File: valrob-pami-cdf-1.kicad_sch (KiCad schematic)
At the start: 111 parts, among them J1 Conn_01x04, J10 Conn_01x04_Pin, J3 USB_C_Receptacle_USB2.0_14P, J4 Conn_01x02, M1 Motor_Servo, Q1 Q_NMOS, Q2 Q_NMOS, Q3 Q_NMOS, SW1 SW_SPST, SW3 SW_Push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

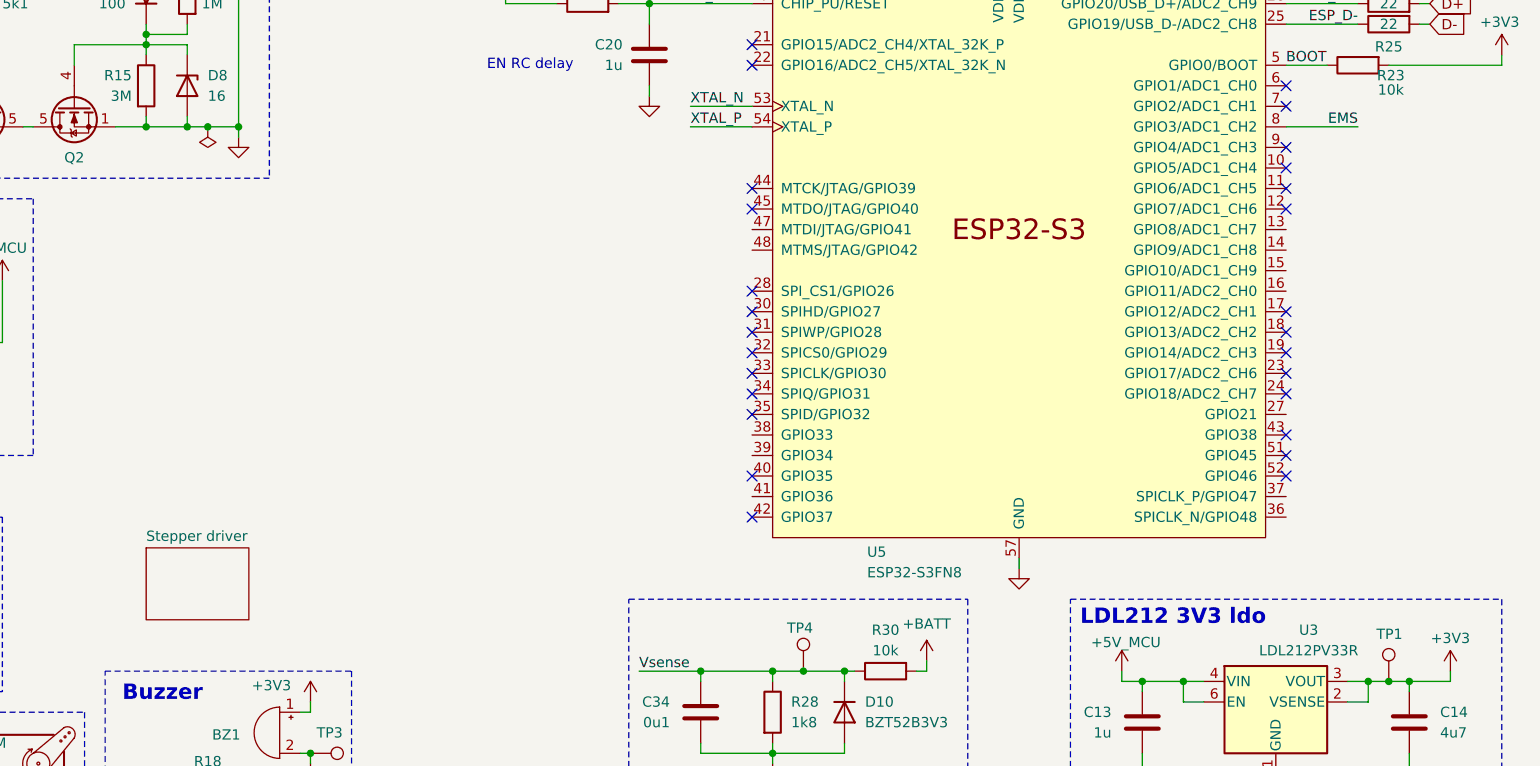
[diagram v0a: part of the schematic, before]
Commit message: schem: fix stepper hierachical sheets
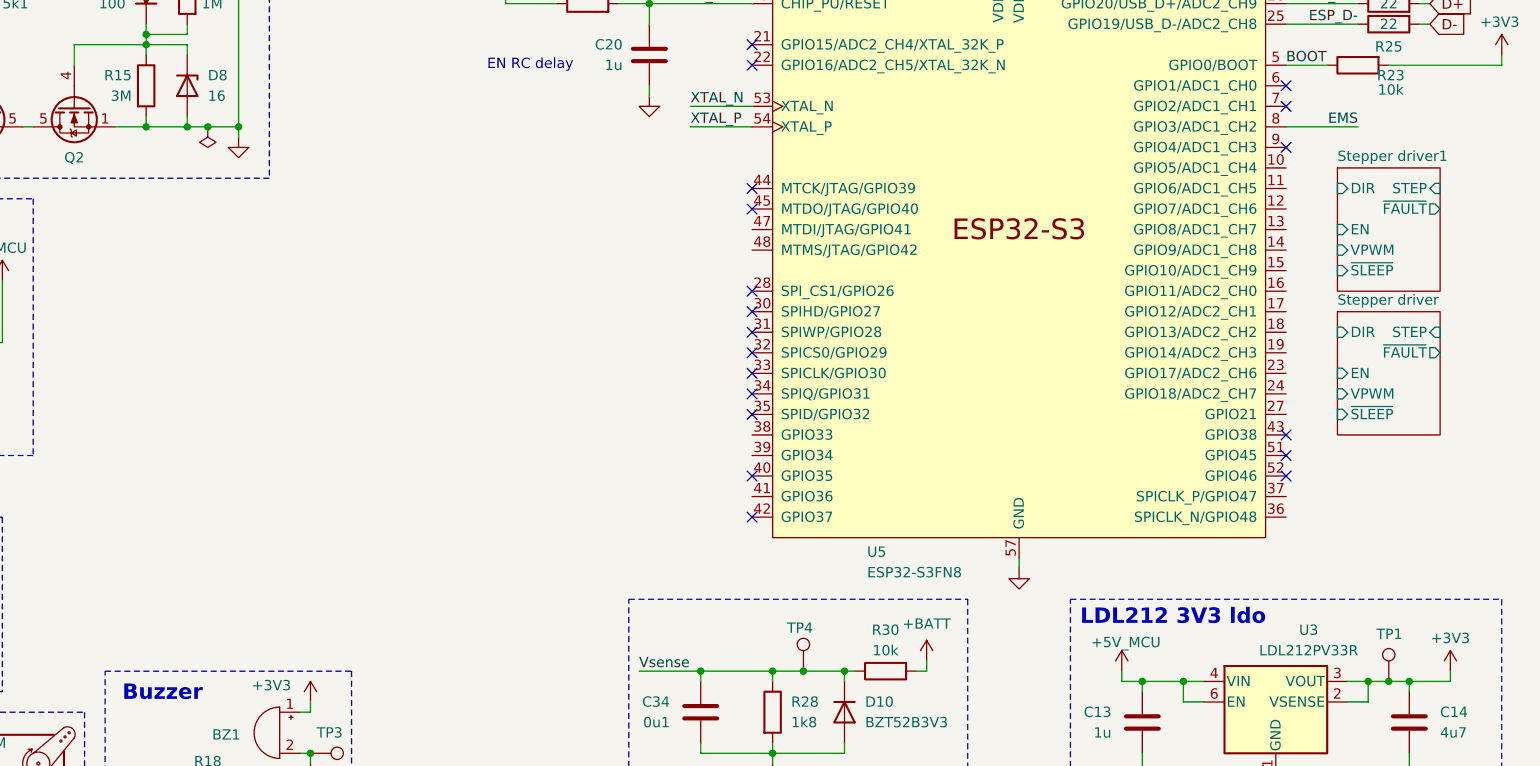
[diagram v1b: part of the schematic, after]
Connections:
- no-connect marks 32 -> 24
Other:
- added sheet Stepper driver1 (stepper.kicad_sch)
- sheet Stepper driver ports: added DIR, EN, STEP, VPWM, ~{FAULT}, ~{SLEEP}; removed none
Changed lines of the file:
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@@
 	)
 	(no_connect
-		(at 255.27 86.36)
-	)
-	(no_connect
 		(at 255.27 81.28)
 	)
@@
 	)
 	(no_connect
-		(at 255.27 101.6)
-	)
-	(no_connect
 		(at 189.23 99.06)
 	)
 	(no_connect
-		(at 255.27 83.82)
-	)
-	(no_connect
 		(at 34.29 107.95)
 	)
@@
 	)
 	(no_connect
-		(at 255.27 111.76)
-	)
-	(no_connect
 		(at 68.58 137.16)
 	)
@@
 	)
 	(no_connect
-		(at 255.27 106.68)
-	)
-	(no_connect
 		(at 189.23 68.58)
 	)
@@
 	)
 	(no_connect
-		(at 255.27 88.9)
-	)
-	(no_connect
-		(at 255.27 109.22)
-	)
-	(no_connect
-		(at 255.27 104.14)
-	)
-	(no_connect
 		(at 88.9 49.53)
 	)
@@
 	)
 	(sheet
-		(at 114.3 130.81)
-		(size 12.7 8.89)
+		(at 261.62 101.6)
+		(size 12.7 15.24)
 		(exclude_from_sim no)
 		(in_bom yes)
@@
 		)
 		(property "Sheetname" "Stepper driver"
-			(at 114.3 130.0984 0)
+			(at 261.62 100.8884 0)
 			(effects
 				(font
@@
 		)
 		(property "Sheetfile" "stepper.kicad_sch"
-			(at 114.3 140.2846 0)
+			(at 261.62 117.4246 0)
 			(effects
 				(font
@@
 			)
 		)
+		(pin "DIR" input
+			(at 261.62 104.14 180)
+			(effects
+				(font
+					(size 1.27 1.27)
+				)
+				(justify left)
+			)
+		)
+		(pin "EN" input
+			(at 261.62 109.22 180)
+			(effects
+				(font
+					(size 1.27 1.27)
+				)
+				(justify left)
+			)
+		)
+		(pin "STEP" input
+			(at 274.32 104.14 0)
+			(effects
+				(font
+					(size 1.27 1.27)
+				)
+				(justify right)
+			)
+		)
+		(pin "VPWM" input
+			(at 261.62 111.76 180)
+			(effects
+				(font
+					(size 1.27 1.27)
+				)
+				(justify left)
+			)
+		)
+		(pin "~{SLEEP}" input
+			(at 261.62 114.3 180)
+			(effects
+				(font
+					(size 1.27 1.27)
+				)
+				(justify left)
+			)
+		)
+		(pin "~{FAULT}" output
+			(at 274.32 106.68 0)
+			(effects
+				(font
+					(size 1.27 1.27)
+				)
+				(justify right)
+			)
+		)
 		(instances
 			(project "valrob-pami-cdf-1"
@@
 				)
 			)
+		)
+	)
+	(sheet
+		(at 261.62 83.82)
+		(size 12.7 15.24)
+		(exclude_from_sim no)
+		(in_bom yes)
+		(on_board yes)
+		(dnp no)
+		(fields_autoplaced yes)
+		(stroke
+			(width 0.1524)
+			(type solid)
+		)
+		(fill
+			(color 0 0 0 0.0000)
+		)
+		(property "Sheetname" "Stepper driver1"
+			(at 261.62 83.1084 0)
+			(effects
+				(font
+					(size 1.27 1.27)
+				)
+				(justify left bottom)
+			)
+		)
+		(property "Sheetfile" "stepper.kicad_sch"
+			(at 261.62 99.6446 0)
+			(effects
+				(font
+					(size 1.27 1.27)
+				)
+				(justify left top)
+				(hide yes)
+			)
+		)
+		(pin "DIR" input
+			(at 261.62 86.36 180)
+			(effects
+				(font
+					(size 1.27 1.27)
+				)
+				(justify left)
+			)
+		)
+		(pin "EN" input
+			(at 261.62 91.44 180)
+			(effects
+				(font
+					(size 1.27 1.27)
+				)
+				(justify left)
+			)
+		)
+		(pin "STEP" input
+			(at 274.32 86.36 0)
+			(effects
+				(font
+					(size 1.27 1.27)
+				)
+				(justify right)
+			)
+		)
+		(pin "VPWM" input
+			(at 261.62 93.98 180)
+			(effects
+				(font
+					(size 1.27 1.27)
+				)
+				(justify left)
+			)
+		)
+		(pin "~{SLEEP}" input
+			(at 261.62 96.52 180)
+			(effects
+				(font
+					(size 1.27 1.27)
+				)
+				(justify left)
+			)
+		)
+		(pin "~{FAULT}" output
+			(at 274.32 88.9 0)
+			(effects
+				(font
+					(size 1.27 1.27)
+				)
+				(justify right)
+			)
+		)
+		(instances
+			(project "valrob-pami-cdf-1"
+				(path "/453def7e-2a78-4c3c-a4b7-f12883e5bdd2"
+					(page "3")
+				)
+			)

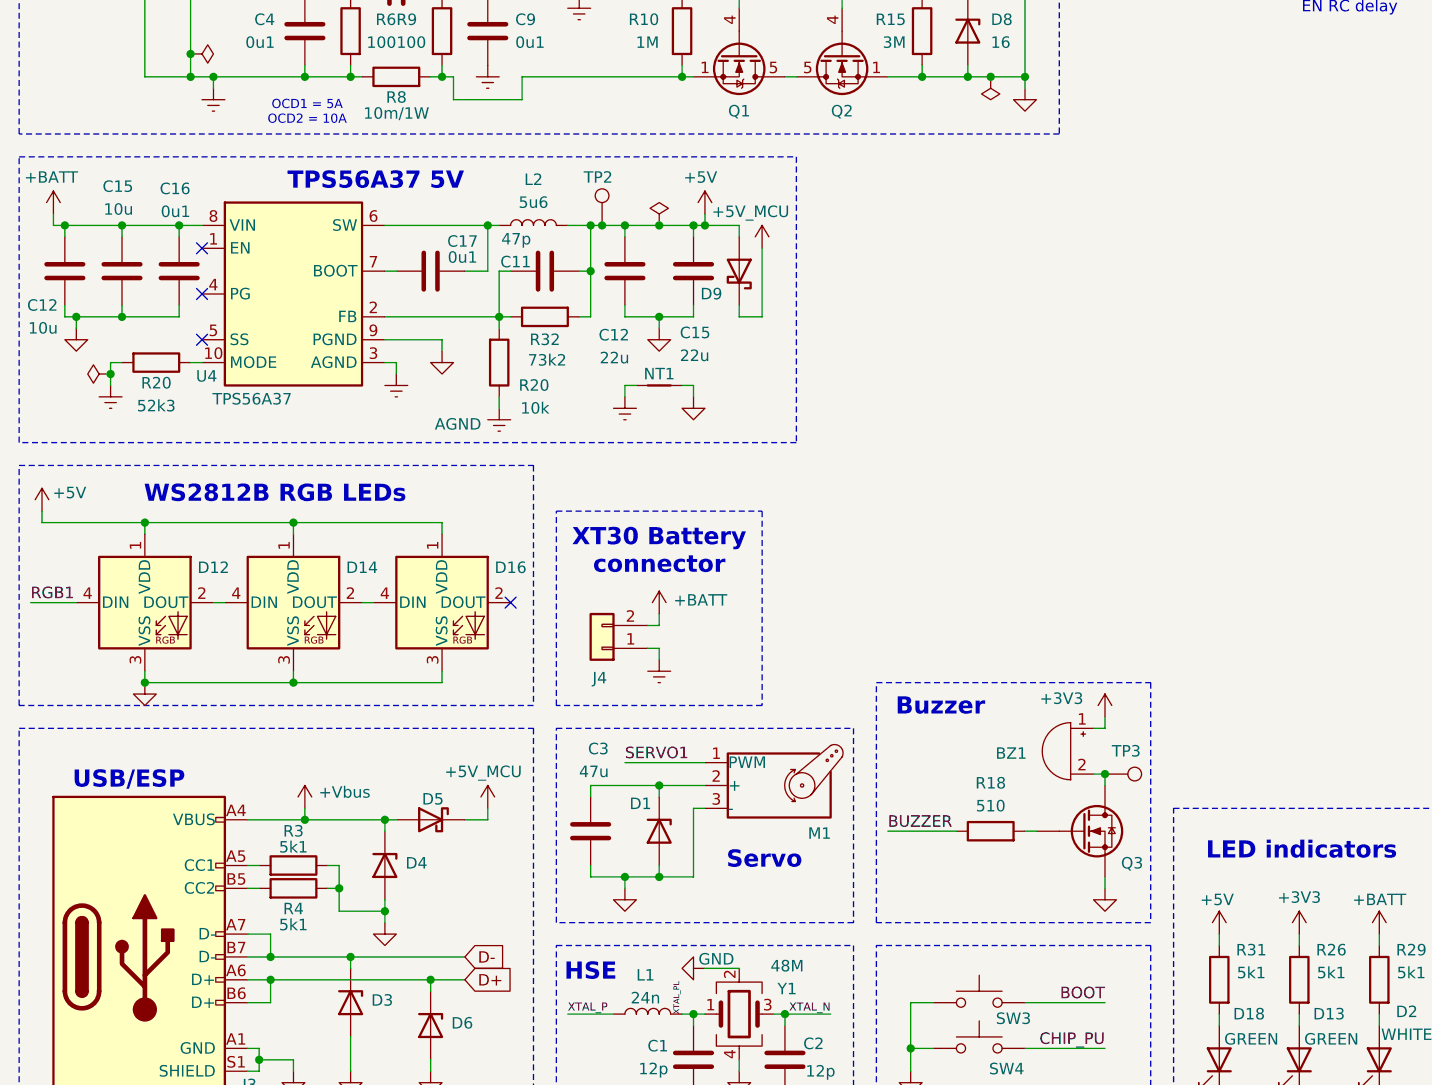
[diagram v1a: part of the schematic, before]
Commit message: schem: change buck converter to TPS62933 5V
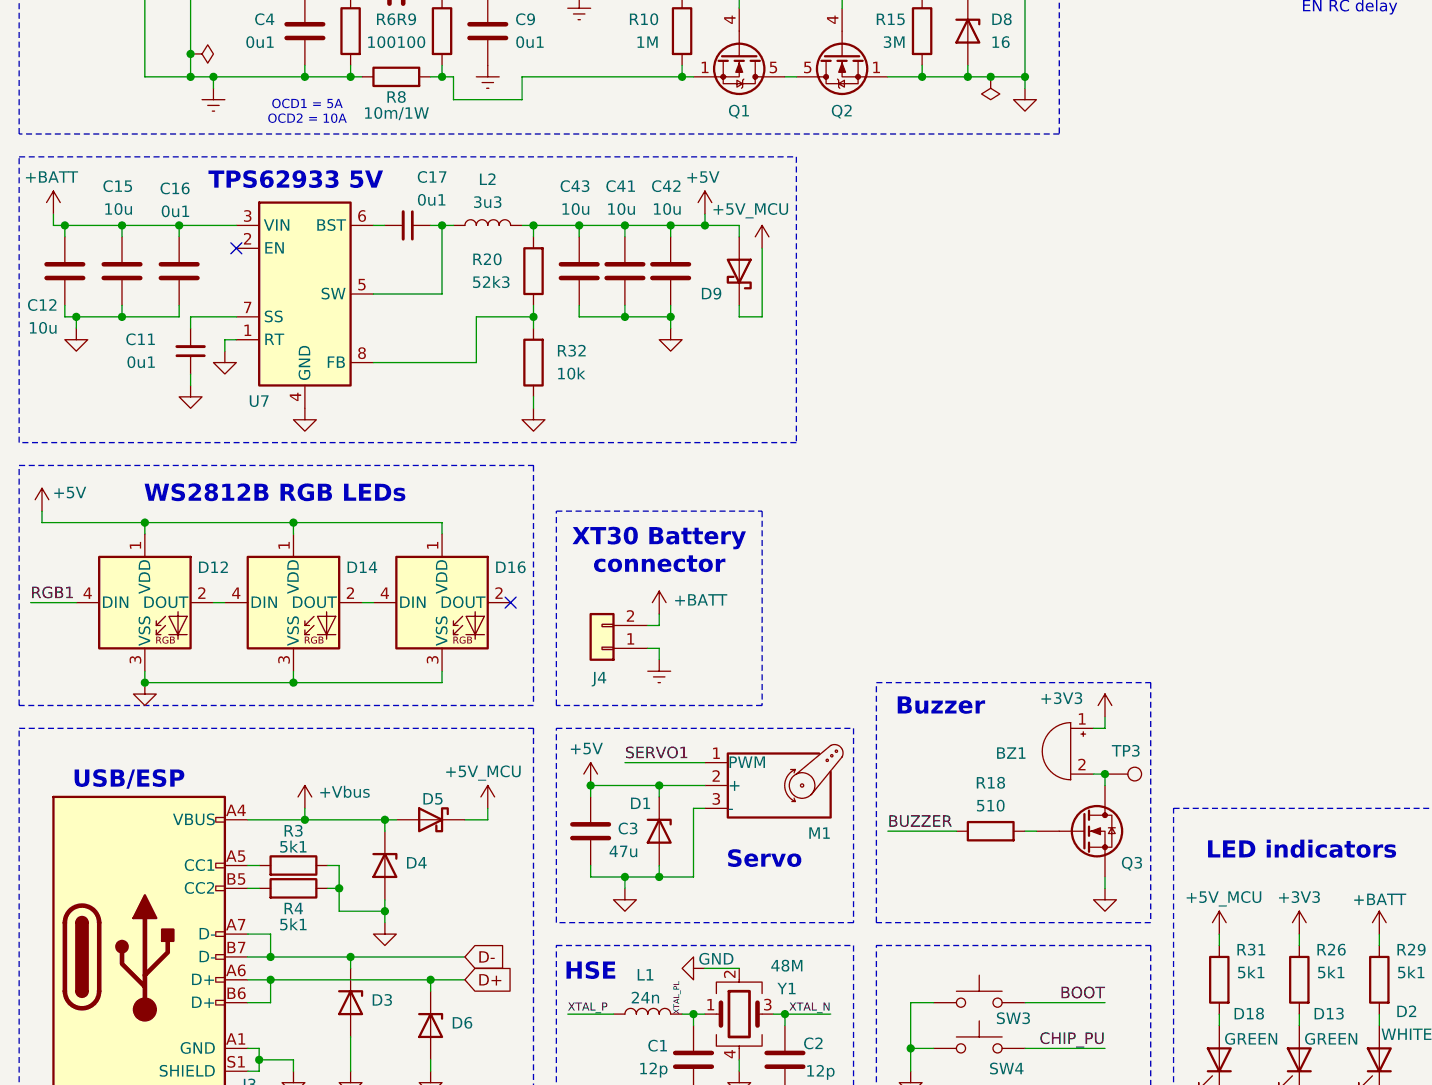
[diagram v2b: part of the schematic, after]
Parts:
- removed C11: 47p, Capacitor_SMD:C_0402_1005Metric, symbol Device:C
- removed C12, C15: 22u, Capacitor_SMD:C_0805_2012Metric, symbol Device:C
- removed C17: 0u1, Capacitor_SMD:C_0402_1005Metric, symbol Device:C
- removed NT1: NetTie_2, NetTie:NetTie-2_SMD_Pad0.5mm, symbol Device:NetTie_2
- removed R20: 10k, Resistor_SMD:R_0402_1005Metric, symbol Device:R
- removed R20: 52k3, Resistor_SMD:R_0402_1005Metric, symbol Device:R
- removed TP2: TestPoint, TestPoint:TestPoint_Pad_D2.0mm, symbol Connector:TestPoint
- removed U4: TPS56A37, GLCS:Texas_RPA0010A_VQFN-HR-10_3x3mm_P0.5mm, symbol GLCS:TPS56A37
- added C11, C17: 0u1, Capacitor_SMD:C_0402_1005Metric, symbol Device:C_Small
- added C41, C42, C43: 10u, Capacitor_SMD:C_0805_2012Metric, symbol Device:C
- added R20: 52k3, Resistor_SMD:R_0402_1005Metric, symbol Device:R
- added U7: TPS62933, Package_TO_SOT_SMD:SOT-583-8, symbol Regulator_Switching:TPS62933
- L2: value 5u6 -> 3u3; footprint Inductor_SMD:L_10.4x10.4_H4.8 -> Inductor_SMD:L_Sunlord_MWSA0402S; JLCPCB Part # C41407183 -> C167207; Manufacturer dehongganying -> cjiang; Manufacturer Part Number DH1040H-5R6M -> FXL0420-3R3-M
- R32: value 73k2 -> 10k; Basic X -> Y; JLCPCB Part # C26986 -> C25744; Manufacturer Part Number 0402WGF7322TCE -> 0402WGF1002TCE
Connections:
- net +5V: now also C3.1, D1.1 (K), M1.2 (+), C41.1, C42.1, C43.1, R20.2; no longer R31.1, R32.2
- net +5V_MCU: now also R31.1
- net +BATT: now also U7.3 (VIN)
- net GND: now also R32.1, C11.1, C41.2, C42.2, C43.2, U7.1 (RT), U7.4 (GND)
- net at L2.1: now also C17.1, U7.5 (SW)
- new net: C17.2, U7.6 (BST)
- new net: C11.2, U7.7 (SS)
- new net: R20.1, R32.2, U7.8 (FB)
- no-connect marks 24 -> 22
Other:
- note added: "TPS62933 5V"
- note removed: "TPS56A37 5V"
